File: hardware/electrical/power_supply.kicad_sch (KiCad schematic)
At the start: 29 parts, among them J4 JST-XH, Q1 IRLZ34N, Q2 IRLZ34N, Q3 IRLML5203, Q4 IRLML5203, Q5 2N7002, Q6 AO3401A, U2 TP4054, U4 WL2803E33-5/TR, U5 AP9101CK6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

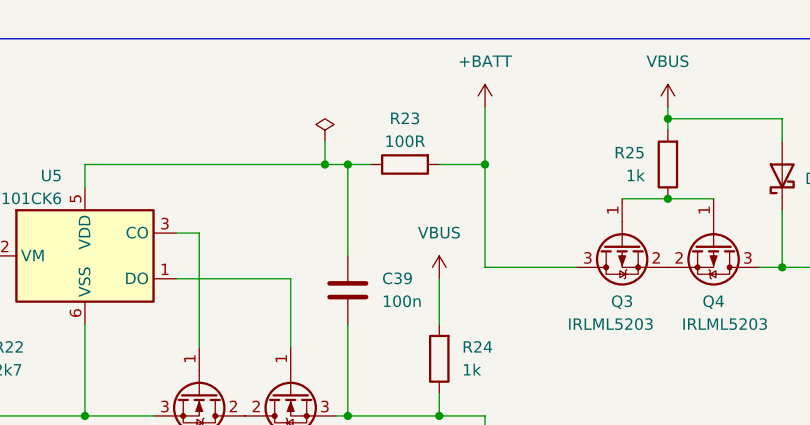
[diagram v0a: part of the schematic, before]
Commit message: changed R23 value
100 -> 330
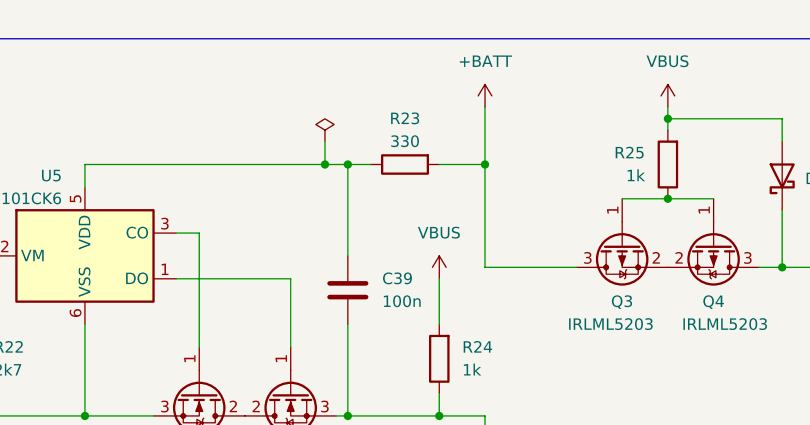
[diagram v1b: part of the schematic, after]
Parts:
- R23: value 100R -> 330
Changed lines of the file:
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@@
       (effects (font (size 1.27 1.27)))
     )
-    (property "Value" "100R" (at 160.02 36.83 90)
+    (property "Value" "330" (at 160.02 36.83 90)
       (effects (font (size 1.27 1.27)))
     )

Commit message: Component selection
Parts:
- removed Q1, Q2: IRLZ34N, Package_TO_SOT_SMD:SOT-23, symbol Transistor_FET:IRLZ34N
- removed Q3, Q4: IRLML5203, Package_TO_SOT_SMD:SOT-23, symbol Transistor_FET:IRLML5203
- added Q1, Q2: AO3400A, Package_TO_SOT_SMD:SOT-23, symbol Transistor_FET:AO3400A
- added Q3, Q4: AO3401A, Package_TO_SOT_SMD:SOT-23, symbol Transistor_FET:AO3401A
- C37, C38: LCSC Part # (none) -> C15525; Mfr (none) -> Samsung Electro-Mechanics; Mfr. Part # (none) -> CL05A106MQ5NUNC
- C39: LCSC Part # (none) -> C1525; Mfr (none) -> Samsung Electro-Mechanics; Mfr. Part # (none) -> CL05B104KO5NNNC
- C40: footprint (none) -> Capacitor_SMD:C_0402_1005Metric; LCSC Part # (none) -> C1525; Mfr (none) -> Samsung Electro-Mechanics; Mfr. Part # (none) -> CL05B104KO5NNNC
- C42, C43: value 10u -> 4u7; LCSC Part # (none) -> C23733; Mfr (none) -> Samsung Electro-Mechanics; Mfr. Part # (none) -> CL05A475MP5NRNC
- D4: footprint Diode_THT:D_DO-41_SOD81_P2.54mm_Vertical_AnodeUp -> Diode_SMD:D_SOD-323; LCSC Part # (none) -> C191023; Mfr (none) -> Guangdong Hottech; Mfr. Part # (none) -> 1N5819WS
- J4: value JST-XH -> JST-PH; footprint (none) -> Connector_JST:JST_PH_S2B-PH-K_1x02_P2.00mm_Horizontal; LCSC Part # (none) -> C173752; Mfr (none) -> JST Sales America; Mfr. Part # (none) -> S2B-PH-K-S(LF)(SN)
- JP2: now left out of the parts list
- Q5: LCSC Part # (none) -> C8545; Mfr (none) -> Changjiang Electronics Tech (CJ); Mfr. Part # (none) -> 2N7002
- Q6: LCSC Part # (none) -> C15127; Mfr (none) -> Alpha & Omega Semicon; Mfr. Part # (none) -> AO3401A
- R19: footprint Resistor_SMD:R_0805_2012Metric_Pad1.20x1.40mm_HandSolder -> Resistor_SMD:R_0603_1608Metric; LCSC Part # (none) -> C4177; Mfr (none) -> UNI-ROYAL(Uniroyal Elec); Mfr. Part # (none) -> 0603WAF1801T5E
- R22: footprint Resistor_SMD:R_0805_2012Metric_Pad1.20x1.40mm_HandSolder -> Resistor_SMD:R_0603_1608Metric; LCSC Part # (none) -> C13167; Mfr (none) -> UNI-ROYAL(Uniroyal Elec); Mfr. Part # (none) -> 0603WAF2701T5E
- R23: footprint Resistor_SMD:R_0805_2012Metric_Pad1.20x1.40mm_HandSolder -> Resistor_SMD:R_0402_1005Metric; LCSC Part # (none) -> C25076; Mfr (none) -> UNI-ROYAL(Uniroyal Elec); Mfr. Part # (none) -> 0402WGF1000TCE
- R24, R25: footprint Resistor_SMD:R_0805_2012Metric_Pad1.20x1.40mm_HandSolder -> Resistor_SMD:R_0402_1005Metric; LCSC Part # (none) -> C11702; Mfr (none) -> UNI-ROYAL(Uniroyal Elec); Mfr. Part # (none) -> 0402WGF1001TCE
- R26, R27: footprint (none) -> Resistor_SMD:R_0402_1005Metric; LCSC Part # (none) -> C25744; Mfr (none) -> UNI-ROYAL(Uniroyal Elec); Mfr. Part # (none) -> 0402WGF1002TCE
- TP1, TP2: footprint TestPoint:TestPoint_Loop_D2.50mm_Drill1.0mm_LowProfile -> (none); now left out of the parts list
- U2: LCSC Part # (none) -> C32574; Mfr (none) -> TOPPOWER(Nanjing Extension Microelectronics); Mfr. Part # (none) -> TP4054-42-SOT25R
- U4: LCSC Part # (none) -> C192928; Mfr (none) -> WILLSEMI(Will Semicon); Mfr. Part # (none) -> WL2803E33-5/TR
- U5: value AP9101CK6 -> AP9101CK6-AYTRG1; LCSC Part # (none) -> C507889; Mfr (none) -> Diodes Incorporated; Mfr. Part # (none) -> AP9101CK6-AYTRG1
- U6: LCSC Part # (none) -> C129757; Mfr (none) -> Diodes Incorporated; Mfr. Part # (none) -> APX803S-31SA-7
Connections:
- net +BATT: now also Q3.3 (D)
- net -BATT: now also Q2.2 (S)
- net GND: now also Q1.2 (S)
- net at U5.1 (DO): now also Q2.1 (G)
- net at R25.1: now also Q3.1 (G), Q4.1 (G)
- net at C42.2, D4.1 (K), U4.1 (IN)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: now also Q4.3 (D)
- net at U5.3 (CO): now also Q1.1 (G)
- new net: Q3.2 (S), Q4.2 (S)
- new net: Q1.3 (D), Q2.3 (D)

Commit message: Add Jushou AFC07-S24ECA-00 footprint and reverse J5 numbering to match camera cable
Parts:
- JP2: footprint (none) -> Jumper:SolderJumper-2_P1.3mm_Open_Pad1.0x1.5mm
- TP1, TP2: footprint (none) -> TestPoint:TestPoint_Pad_D1.5mm
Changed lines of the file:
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@@
       (effects (font (size 1.27 1.27)) (justify left) hide)
     )
-    (property "Footprint" "" (at 237.49 87.63 0)
+    (property "Footprint" "Jumper:SolderJumper-2_P1.3mm_Open_Pad1.0x1.5mm" (at 237.49 87.63 0)
       (effects (font (size 1.27 1.27)) hide)
     )
@@
       (effects (font (size 1.27 1.27)) (justify left) hide)
     )
-    (property "Footprint" "" (at 67.31 102.87 0)
+    (property "Footprint" "TestPoint:TestPoint_Pad_D1.5mm" (at 67.31 102.87 0)
       (effects (font (size 1.27 1.27)) hide)
     )
@@
       (effects (font (size 1.27 1.27)) (justify left) hide)
     )
-    (property "Footprint" "" (at 67.31 100.33 0)
-      (effects (font (size 1.27 1.27)) hide)
-    )
+    (property "Footprint" "TestPoint:TestPoint_Pad_D1.5mm" (at 67.31 100.33 0)
+      (effects (font (size 1.27 1.27)) hide)
+    )

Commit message: Change R23 part no.
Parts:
- R23: LCSC Part # C25076 -> C25104; Mfr. Part # 0402WGF1000TCE -> 0402WGF3300TCE
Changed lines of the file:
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@@
       (effects (font (size 1.27 1.27)) hide)
     )
-    (property "LCSC Part #" "C25076" (at 160.02 39.37 0)
+    (property "LCSC Part #" "C25104" (at 160.02 39.37 0)
       (effects (font (size 1.27 1.27)) hide)
     )
@@
       (effects (font (size 1.27 1.27)) hide)
     )
-    (property "Mfr. Part #" "0402WGF1000TCE" (at 160.02 39.37 0)
+    (property "Mfr. Part #" "0402WGF3300TCE" (at 160.02 39.37 0)
       (effects (font (size 1.27 1.27)) hide)
     )

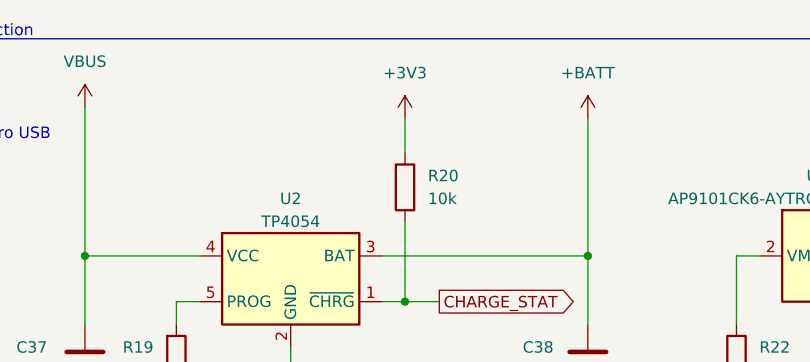
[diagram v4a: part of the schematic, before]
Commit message: Revise power supply
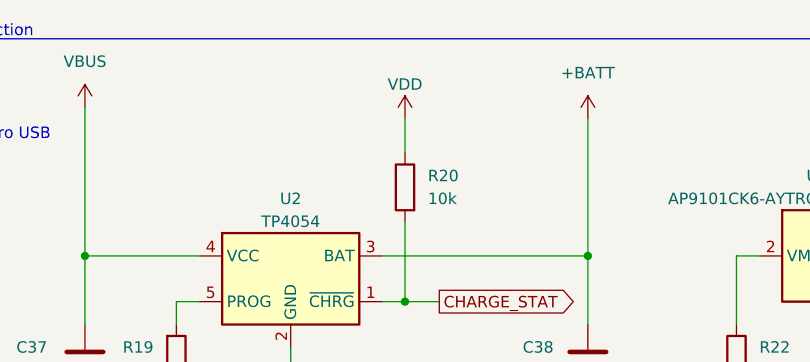
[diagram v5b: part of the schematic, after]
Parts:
- TP1, TP2: footprint TestPoint:TestPoint_Pad_D1.5mm -> TestPoint:TestPoint_Pad_D1.0mm
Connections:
- net +3V3: no longer R20.1
- net VDD: now also R20.1
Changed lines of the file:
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@@
-    )
-  )
-  (symbol (lib_id "power:+3V3") (at 74.93 34.29 0) (unit 1)
-    (in_bom yes) (on_board yes) (dnp no)
-    (property "Reference" "#PWR0101" (at 74.93 38.1 0)
-      (effects (font (size 1.27 1.27)) hide)
-    )
-    (property "Value" "+3V3" (at 74.93 29.21 0)
-      (effects (font (size 1.27 1.27)))
-    )
-    (property "Footprint" "" (at 74.93 34.29 0)
-      (effects (font (size 1.27 1.27)) hide)
-    )
-    (property "Datasheet" "" (at 74.93 34.29 0)
-      (effects (font (size 1.27 1.27)) hide)
-    )
-    (pin "1")
-    (instances
-      (project "3885"
-        (path "/7363a4f0-2da1-4086-abed-ea6709c3a185/0217b7ef-3928-43d6-9a5a-467bfde0e5ea"
-          (reference "#PWR0101") (unit 1)
-        )
-      )
     )
   )
@@
       (effects (font (size 1.27 1.27)) (justify left) hide)
     )
-    (property "Footprint" "TestPoint:TestPoint_Pad_D1.5mm" (at 67.31 102.87 0)
+    (property "Footprint" "TestPoint:TestPoint_Pad_D1.0mm" (at 67.31 102.87 0)
       (effects (font (size 1.27 1.27)) hide)
     )
@@
       (effects (font (size 1.27 1.27)) (justify left) hide)
     )
-    (property "Footprint" "TestPoint:TestPoint_Pad_D1.5mm" (at 67.31 100.33 0)
+    (property "Footprint" "TestPoint:TestPoint_Pad_D1.0mm" (at 67.31 100.33 0)
       (effects (font (size 1.27 1.27)) hide)
     )
@@
         )
       )
+    )
+  )
+  (symbol (lib_id "power:VDD") (at 74.93 34.29 0) (unit 1)
+    (in_bom yes) (on_board yes) (dnp no) (fields_autoplaced)
+    (property "Reference" "#PWR027" (at 74.93 38.1 0)
+      (effects (font (size 1.27 1.27)) hide)
+    )
+    (property "Value" "VDD" (at 74.93 30.48 0)
+      (effects (font (size 1.27 1.27)))
+    )
+    (property "Footprint" "" (at 74.93 34.29 0)
+      (effects (font (size 1.27 1.27)) hide)
+    )
+    (property "Datasheet" "" (at 74.93 34.29 0)
+      (effects (font (size 1.27 1.27)) hide)
+    )
+    (pin "1")
+    (instances
+      (project "3885"
+        (path "/7363a4f0-2da1-4086-abed-ea6709c3a185/0217b7ef-3928-43d6-9a5a-467bfde0e5ea"
+          (reference "#PWR027") (unit 1)
+        )
+      )

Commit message: Implement James' recommendations
* Move R22 GND via out of -BATT fill
* Remove TP1 from schematic
* Remove TP2 from schematic
* Remove JP2 from schematic
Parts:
- removed JP2: Jumper_2_Open, Jumper:SolderJumper-2_P1.3mm_Open_Pad1.0x1.5mm, symbol Jumper:Jumper_2_Open
- removed TP1: TestPoint, TestPoint:TestPoint_Pad_D1.0mm, symbol Connector:TestPoint
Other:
- note removed: "3V3 test point"
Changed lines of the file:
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@@
   (junction (at 153.67 39.37) (diameter 0) (color 0 0 0 0)
   )
-  (junction (at 248.92 99.06) (diameter 0) (color 0 0 0 0)
-  )
   (junction (at 49.53 67.31) (diameter 0) (color 0 0 0 0)
   )
@@
   (junction (at 168.91 39.37) (diameter 0) (color 0 0 0 0)
   )
-  (junction (at 222.25 99.06) (diameter 0) (color 0 0 0 0)
-  )
   (junction (at 39.37 67.31) (diameter 0) (color 0 0 0 0)
   )
@@
     (stroke (width 0) (type default))
   )
-  (wire (pts (xy 232.41 87.63) (xy 222.25 87.63))
-    (stroke (width 0) (type default))
-  )
   (wire (pts (xy 39.37 49.53) (xy 39.37 57.15))
     (stroke (width 0) (type default))
@@
     (stroke (width 0) (type default))
   )
-  (wire (pts (xy 64.77 95.25) (xy 67.31 95.25))
-    (stroke (width 0) (type default))
-  )
   (wire (pts (xy 227.33 50.8) (xy 227.33 53.34))
     (stroke (width 0) (type default))
@@
     (stroke (width 0) (type default))
   )
-  (wire (pts (xy 222.25 99.06) (xy 224.79 99.06))
+  (wire (pts (xy 219.71 99.06) (xy 224.79 99.06))
     (stroke (width 0) (type default))
   )
@@
     (stroke (width 0) (type default))
   )
-  (wire (pts (xy 248.92 99.06) (xy 252.73 99.06))
-    (stroke (width 0) (type default))
-  )
-  (wire (pts (xy 242.57 87.63) (xy 248.92 87.63))
+  (wire (pts (xy 242.57 99.06) (xy 252.73 99.06))
     (stroke (width 0) (type default))
   )
@@
     (stroke (width 0) (type default))
   )
-  (wire (pts (xy 248.92 87.63) (xy 248.92 99.06))
-    (stroke (width 0) (type default))
-  )
   (wire (pts (xy 168.91 67.31) (xy 168.91 69.85))
     (stroke (width 0) (type default))
   )
-  (wire (pts (xy 64.77 92.71) (xy 64.77 95.25))
-    (stroke (width 0) (type default))
-  )
   (polyline (pts (xy 17.78 25.4) (xy 212.09 25.4))
     (stroke (width 0) (type default))
@@
     (stroke (width 0) (type default))
   )
-  (wire (pts (xy 222.25 87.63) (xy 222.25 99.06))
-    (stroke (width 0) (type default))
-  )
   (polyline (pts (xy 212.09 77.47) (xy 17.78 77.47))
     (stroke (width 0) (type default))
@@
     (stroke (width 0) (type default))
   )
-  (wire (pts (xy 242.57 99.06) (xy 248.92 99.06))
-    (stroke (width 0) (type default))
-  )
   (wire (pts (xy 39.37 95.25) (xy 48.26 95.25))
     (stroke (width 0) (type default))
@@
   )
   (wire (pts (xy 62.23 67.31) (xy 95.25 67.31))
-    (stroke (width 0) (type default))
-  )
-  (wire (pts (xy 219.71 99.06) (xy 222.25 99.06))
     (stroke (width 0) (type default))
   )
@@
   )
   (text "Battery Protection" (at 17.78 25.4 0)
-    (effects (font (size 1.27 1.27)) (justify left bottom))
-  )
-  (text "3V3 test point" (at 60.96 85.09 0)
     (effects (font (size 1.27 1.27)) (justify left bottom))
   )
@@
     )
   )
-  (symbol (lib_id "Jumper:Jumper_2_Open") (at 237.49 87.63 0) (unit 1)
-    (in_bom no) (on_board yes) (dnp no)
-    (property "Reference" "JP2" (at 237.49 83.82 0)
-      (effects (font (size 1.27 1.27)))
-    )
-    (property "Value" "Jumper_2_Open" (at 238.7599 85.09 90)
-      (effects (font (size 1.27 1.27)) (justify left) hide)
-    )
-    (property "Footprint" "Jumper:SolderJumper-2_P1.3mm_Open_Pad1.0x1.5mm" (at 237.49 87.63 0)
-      (effects (font (size 1.27 1.27)) hide)
-    )
-    (property "Datasheet" "~" (at 237.49 87.63 0)
-      (effects (font (size 1.27 1.27)) hide)
-    )
-    (pin "1")
-    (pin "2")
-    (instances
-      (project "3885"
-        (path "/7363a4f0-2da1-4086-abed-ea6709c3a185/0217b7ef-3928-43d6-9a5a-467bfde0e5ea"
-          (reference "JP2") (unit 1)
-        )
-      )
-    )
-  )
   (symbol (lib_id "power:VBUS") (at 39.37 33.02 0) (unit 1)
     (in_bom yes) (on_board yes) (dnp no) (fields_autoplaced)
@@
         (path "/7363a4f0-2da1-4086-abed-ea6709c3a185/0217b7ef-3928-43d6-9a5a-467bfde0e5ea"
           (reference "#PWR067") (unit 1)
-        )
-      )
-    )
-  )
-  (symbol (lib_id "Connector:TestPoint") (at 67.31 95.25 270) (unit 1)
-    (in_bom no) (on_board yes) (dnp no)
-    (property "Reference" "TP1" (at 74.93 95.25 90)
-      (effects (font (size 1.27 1.27)))
-    )
-    (property "Value" "TestPoint" (at 69.3421 97.79 0)
-      (effects (font (size 1.27 1.27)) (justify left) hide)
-    )
-    (property "Footprint" "TestPoint:TestPoint_Pad_D1.0mm" (at 67.31 100.33 0)
-      (effects (font (size 1.27 1.27)) hide)
-    )
-    (property "Datasheet" "~" (at 67.31 100.33 0)
-      (effects (font (size 1.27 1.27)) hide)
-    )
-    (pin "1")
-    (instances
-      (project "3885"
-        (path "/7363a4f0-2da1-4086-abed-ea6709c3a185/0217b7ef-3928-43d6-9a5a-467bfde0e5ea"
-          (reference "TP1") (unit 1)
         )
       )
@@
         )
       )
-    )
-  )
-  (symbol (lib_id "power:+3V3") (at 64.77 92.71 0) (unit 1)
-    (in_bom yes) (on_board yes) (dnp no)
-    (property "Reference" "#PWR070" (at 64.77 96.52 0)
-      (effects (font (size 1.27 1.27)) hide)
-    )
-    (property "Value" "+3V3" (at 64.77 87.63 0)
-      (effects (font (size 1.27 1.27)))
-    )
-    (property "Footprint" "" (at 64.77 92.71 0)
-      (effects (font (size 1.27 1.27)) hide)
-    )
-    (property "Datasheet" "" (at 64.77 92.71 0)
-      (effects (font (size 1.27 1.27)) hide)
-    )
-    (pin "1")
-    (instances
-      (project "3885"
-        (path "/7363a4f0-2da1-4086-abed-ea6709c3a185/0217b7ef-3928-43d6-9a5a-467bfde0e5ea"
-          (reference "#PWR070") (unit 1)
-        )
-      )

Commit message: Increase clearances to pass stricter DRC
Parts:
- removed TP2: TestPoint, TestPoint:TestPoint_Pad_D1.0mm, symbol Connector:TestPoint
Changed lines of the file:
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@@
-    (stroke (width 0) (type default))
-  )
-  (wire (pts (xy 64.77 97.79) (xy 67.31 97.79))
     (stroke (width 0) (type default))
   )
@@
   )
   (wire (pts (xy 124.46 67.31) (xy 132.08 67.31))
-    (stroke (width 0) (type default))
-  )
-  (wire (pts (xy 64.77 97.79) (xy 64.77 100.33))
     (stroke (width 0) (type default))
   )
@@
     )
   )
-  (symbol (lib_id "Connector:TestPoint") (at 67.31 97.79 270) (unit 1)
-    (in_bom no) (on_board yes) (dnp no)
-    (property "Reference" "TP2" (at 74.93 97.79 90)
-      (effects (font (size 1.27 1.27)))
-    )
-    (property "Value" "TestPoint" (at 69.3421 100.33 0)
-      (effects (font (size 1.27 1.27)) (justify left) hide)
-    )
-    (property "Footprint" "TestPoint:TestPoint_Pad_D1.0mm" (at 67.31 102.87 0)
-      (effects (font (size 1.27 1.27)) hide)
-    )
-    (property "Datasheet" "~" (at 67.31 102.87 0)
-      (effects (font (size 1.27 1.27)) hide)
-    )
-    (pin "1")
-    (instances
-      (project "3885"
-        (path "/7363a4f0-2da1-4086-abed-ea6709c3a185/0217b7ef-3928-43d6-9a5a-467bfde0e5ea"
-          (reference "TP2") (unit 1)
-        )
-      )
-    )
-  )
   (symbol (lib_id "Transistor_FET:AO3400A") (at 147.32 64.77 90) (mirror x) (unit 1)
     (in_bom yes) (on_board yes) (dnp no)
@@
         )
       )
-    )
-  )
-  (symbol (lib_id "power:GND") (at 64.77 100.33 0) (unit 1)
-    (in_bom yes) (on_board yes) (dnp no)
-    (property "Reference" "#PWR071" (at 64.77 106.68 0)
-      (effects (font (size 1.27 1.27)) hide)
-    )
-    (property "Value" "GND" (at 64.77 105.41 0)
-      (effects (font (size 1.27 1.27)))
-    )
-    (property "Footprint" "" (at 64.77 100.33 0)
-      (effects (font (size 1.27 1.27)) hide)
-    )
-    (property "Datasheet" "" (at 64.77 100.33 0)
-      (effects (font (size 1.27 1.27)) hide)
-    )
-    (pin "1")
-    (instances
-      (project "3885"
-        (path "/7363a4f0-2da1-4086-abed-ea6709c3a185/0217b7ef-3928-43d6-9a5a-467bfde0e5ea"
-          (reference "#PWR071") (unit 1)
-        )
-      )

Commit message: Connect U5 VSS to -BATT instead of GND
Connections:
- net -BATT: now also U5.6 (VSS)
- net GND: no longer U5.6 (VSS)
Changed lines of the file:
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@@
 (kicad_sch (version 20230121) (generator eeschema)
   (paper "A4")
+  (title_block
+    (rev "2.2")
+  )
   (junction (at 111.76 67.31) (diameter 0) (color 0 0 0 0)
   )
@@
   (junction (at 204.47 99.06) (diameter 0) (color 0 0 0 0)
   )
-  (junction (at 124.46 67.31) (diameter 0) (color 0 0 0 0)
-  )
   (junction (at 224.79 50.8) (diameter 0) (color 0 0 0 0)
   )
@@
     (stroke (width 0) (type default))
   )
-  (wire (pts (xy 124.46 67.31) (xy 132.08 67.31))
-    (stroke (width 0) (type default))
-  )
   (wire (pts (xy 124.46 39.37) (xy 151.13 39.37))
     (stroke (width 0) (type default))
@@
     (stroke (width 0) (type default))
   )
+  (wire (pts (xy 124.46 57.15) (xy 124.46 69.85))
+    (stroke (width 0) (type default))
+  )
   (polyline (pts (xy 215.9 77.47) (xy 262.89 77.47))
     (stroke (width 0) (type default))
@@
     (stroke (width 0) (type default))
   )
-  (wire (pts (xy 111.76 67.31) (xy 124.46 67.31))
+  (wire (pts (xy 111.76 67.31) (xy 132.08 67.31))
     (stroke (width 0) (type default))
   )
@@
   )
   (polyline (pts (xy 269.24 73.66) (xy 215.9 73.66))
-    (stroke (width 0) (type default))
-  )
-  (wire (pts (xy 124.46 57.15) (xy 124.46 67.31))
     (stroke (width 0) (type default))
   )
@@
         )
       )
+    )
+  )
+  (symbol (lib_id "power:-BATT") (at 124.46 69.85 180) (unit 1)
+    (in_bom yes) (on_board yes) (dnp no) (fields_autoplaced)
+    (property "Reference" "#PWR029" (at 124.46 66.04 0)
+      (effects (font (size 1.27 1.27)) hide)
+    )
+    (property "Value" "-BATT" (at 124.46 74.93 0)
+      (effects (font (size 1.27 1.27)))
+    )
+    (property "Footprint" "" (at 124.46 69.85 0)
+      (effects (font (size 1.27 1.27)) hide)
+    )
+    (property "Datasheet" "" (at 124.46 69.85 0)
+      (effects (font (size 1.27 1.27)) hide)
+    )
+    (pin "1")
+    (instances
+      (project "3885"
+        (path "/7363a4f0-2da1-4086-abed-ea6709c3a185/0217b7ef-3928-43d6-9a5a-467bfde0e5ea"
+          (reference "#PWR029") (unit 1)
+        )
+      )
